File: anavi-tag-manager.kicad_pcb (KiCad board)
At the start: 2 copper layers, 74.9 x 40.6 mm, 22 parts, among them P1 CONN_01X03, U1 I2C_SENS_1, U2 I2C_SENS_1, U3 I2C_SENS_1

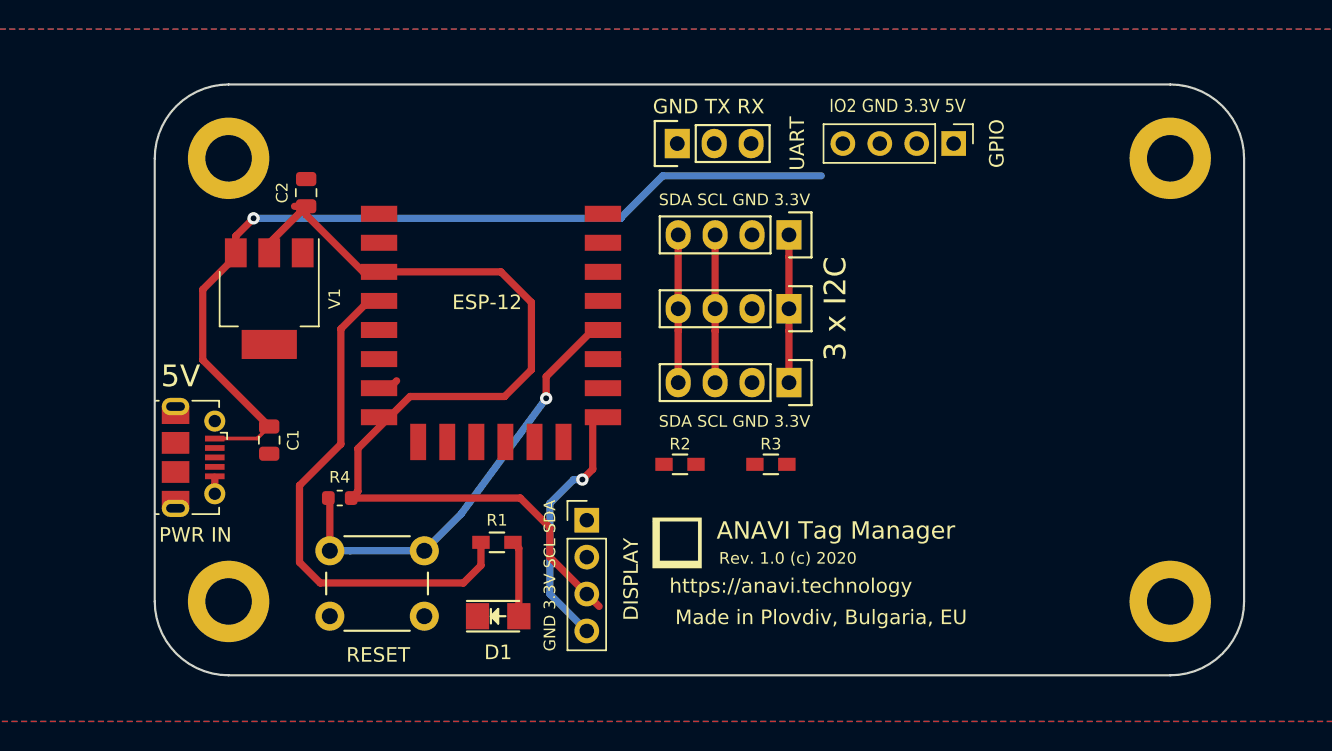
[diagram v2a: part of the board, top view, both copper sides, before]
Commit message: anavi-tag-manager.kicad_pcb: Import netlist
Signed-off-by: Leon Anavi <leon@anavi.org>
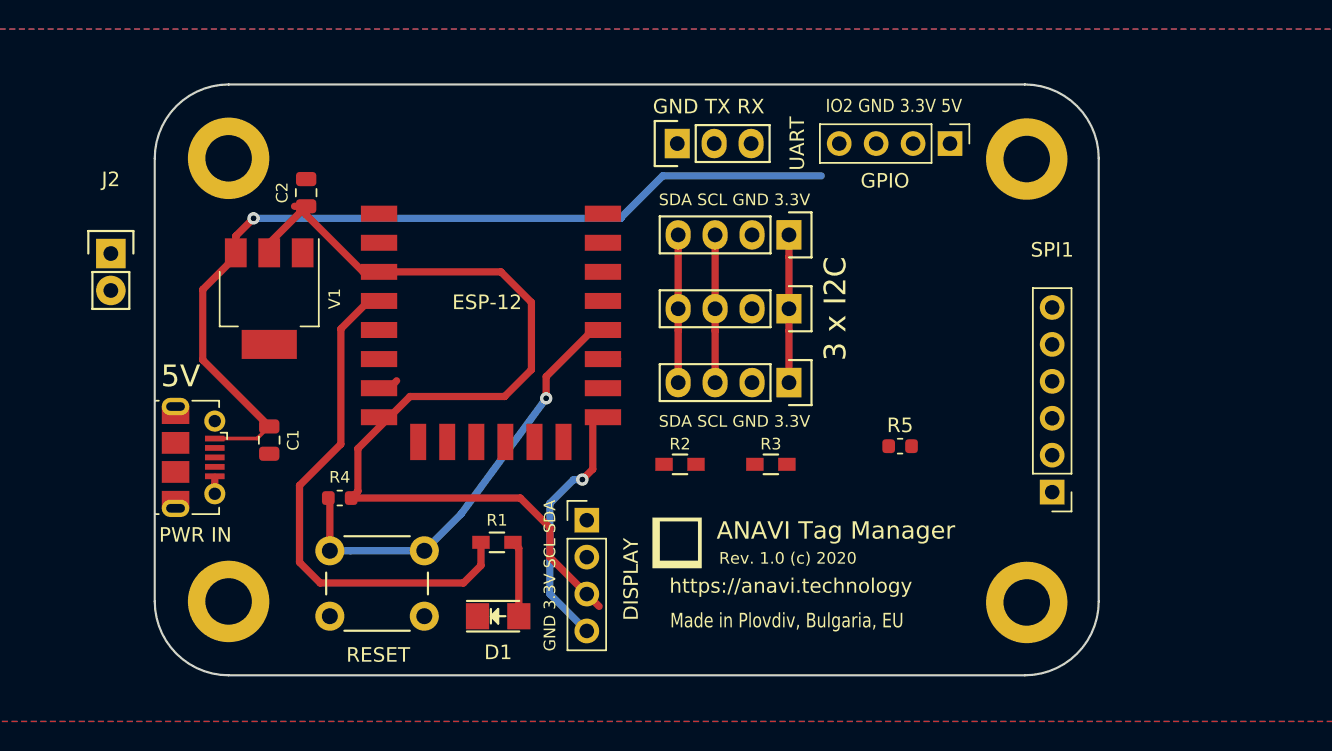
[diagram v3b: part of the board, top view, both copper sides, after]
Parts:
- removed the REF** at (134.6, 76.2)
- removed the REF** at (134.6, 106.7)
- added J2: Conn_01x02, Pin_Headers:Pin_Header_Straight_1x02, F.Cu at (61.8, 82.8)
- added R5: 4,7K, Resistor_SMD:R_0603_1608Metric, F.Cu at (116.0, 96.0)
- added REF**: MountingHole_3.2mm_M3_DIN965_Pad, Mounting_Holes:MountingHole_3.2mm_M3_DIN965_Pad, F.Cu at (124.8, 76.2)
- added REF**: MountingHole_3.2mm_M3_DIN965_Pad, Mounting_Holes:MountingHole_3.2mm_M3_DIN965_Pad, F.Cu at (124.8, 106.8)
- added SPI1: Conn_01x06, Connector_PinHeader_2.54mm:PinHeader_1x06_P2.54mm_Vertical, F.Cu at (126.5, 99.2)
- moved GPIO 0.25 mm to (119.5, 75.2)
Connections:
- ESP-12 pad 1: Net-(ESP-12-Pad1) -> (no net)
- ESP-12 pad 10: GND -> Net-(ESP-12-Pad10)
- ESP-12 pad 17: Net-(ESP-12-Pad17) -> (no net)
- ESP-12 pad 18: Net-(ESP-12-Pad18) -> (no net)
- ESP-12 pad 19: Net-(ESP-12-Pad19) -> (no net)
- ESP-12 pad 2: Net-(ESP-12-Pad2) -> (no net)
- ESP-12 pad 20: Net-(ESP-12-Pad20) -> (no net)
- ESP-12 pad 21: Net-(ESP-12-Pad21) -> (no net)
- ESP-12 pad 22: Net-(ESP-12-Pad22) -> (no net)
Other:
- board size 74.9 x 40.6 mm -> 64.9 x 40.6 mm

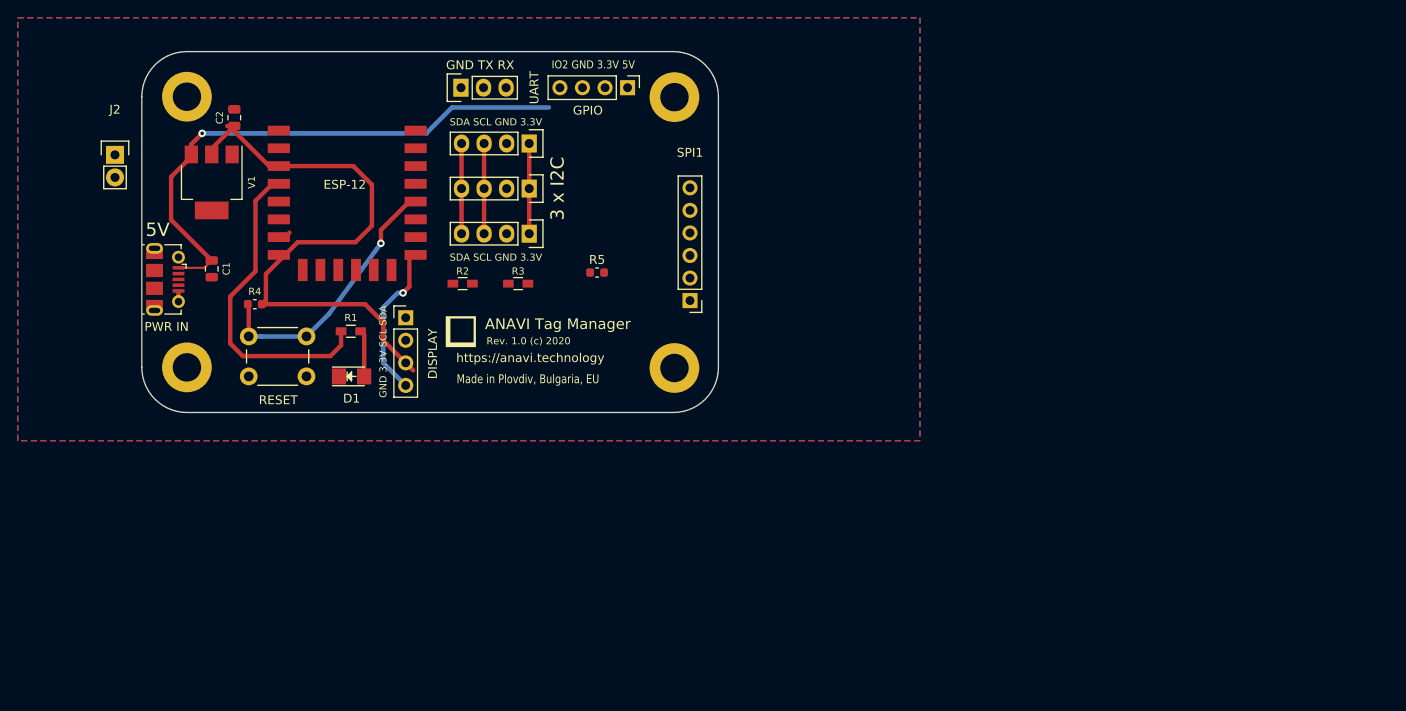
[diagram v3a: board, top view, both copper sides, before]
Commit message: anavi-tag-manager.kicad_pcb: PCB routing
Apart from the routing, also change the position of GND on the
GPIO header (with IO2). The new order makes connecting servo
motors easier because the yellow wire should go to IO2, red wire
to 5V and black wire to GND.

Signed-off-by: Leon Anavi <leon@anavi.org>
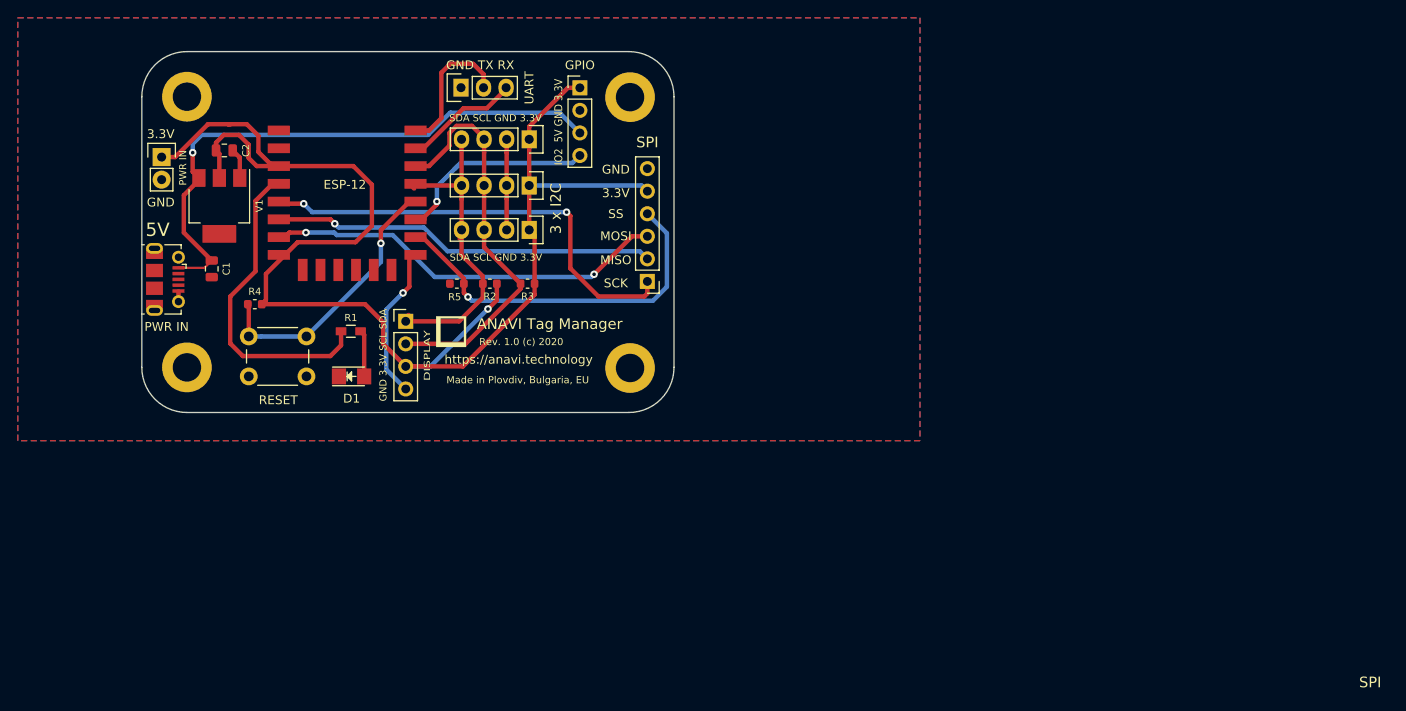
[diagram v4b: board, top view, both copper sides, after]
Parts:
- removed SPI1: Conn_01x06, Connector_PinHeader_2.54mm:PinHeader_1x06_P2.54mm_Vertical
- added ?: , , F.Cu at (121.8, 81.0)
- added SPI: Conn_01x06, Connector_PinHeader_2.54mm:PinHeader_1x06_P2.54mm_Vertical, F.Cu at (121.7, 97.0)
- PWR IN: renamed from J2
- R2, R3: footprint Resistors_SMD:R_0603_HandSoldering -> Resistor_SMD:R_0603_1608Metric
- moved R5 15.8 mm to (100.2, 97.2), turned to 180 degrees
- moved GPIO 5.37 mm to (114.1, 75.2), turned to 0 degrees
- moved PWR IN 5.26 mm to (67.0, 83.0)
- moved REF** 5.00 mm to (119.8, 76.2)
- moved REF** 5.00 mm to (119.8, 106.8)
- moved C2 3.85 mm to (74.1, 82.2), turned to 0 degrees
- moved R2 3.06 mm to (104.0, 97.3)
- moved V1 2.78 mm to (73.5, 88.5)
- moved G*** 1.10 mm to (99.6, 102.7)
- moved R3 1.06 mm to (108.2, 97.3)
- moved U3 0.47 mm to (108.4, 81.0)
- moved U1 0.43 mm to (108.4, 91.2)
- moved DISPLAY 0.40 mm to (94.5, 101.5)
- moved U2 0.35 mm to (108.4, 86.2)
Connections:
- GPIO pad 1: +5V -> +3V3
- GPIO pad 2: +3V3 -> GND
- GPIO pad 3: GND -> +5V
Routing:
- net +3V3: track 77.9 -> 163.2 mm, vias 0 -> 1
- net Net-(ESP-12-Pad5): track 0.00 -> 50.2 mm, vias 0 -> 2
- net Net-(ESP-12-Pad7): track 0.72 -> 45.7 mm, vias 0 -> 2
- net Net-(ESP-12-Pad10): track 0.00 -> 44.1 mm, vias 0 -> 1
- net Net-(ESP-12-Pad6): track 0.00 -> 42.6 mm, vias 0 -> 1
- net Net-(ESP-12-Pad14): track 10.5 -> 47.4 mm
- net Net-(ESP-12-Pad13): track 11.2 -> 36.4 mm
- net Net-(ESP-12-Pad11): track 3.12 -> 25.5 mm, vias 0 -> 1
- net Net-(ESP-12-Pad16): track 0.00 -> 16.5 mm
- net Net-(ESP-12-Pad15): track 0.00 -> 13.8 mm
- net GND: track 18.5 -> 31.9 mm
- net +5V: track 62.6 -> 66.0 mm
- net Net-(ESP-12-Pad12): track 29.7 -> 30.2 mm
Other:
- board size 64.9 x 40.6 mm -> 59.9 x 40.6 mm
- board text added: "3.3V"
- board text added: "GND"
- board text added: "IO2 5V GND 3.3V"
- board text added: "MISO"
- board text added: "MOSI"
- board text added: "SCK"
- board text added: "SS"
- board text removed: "IO2 GND 3.3V 5V"

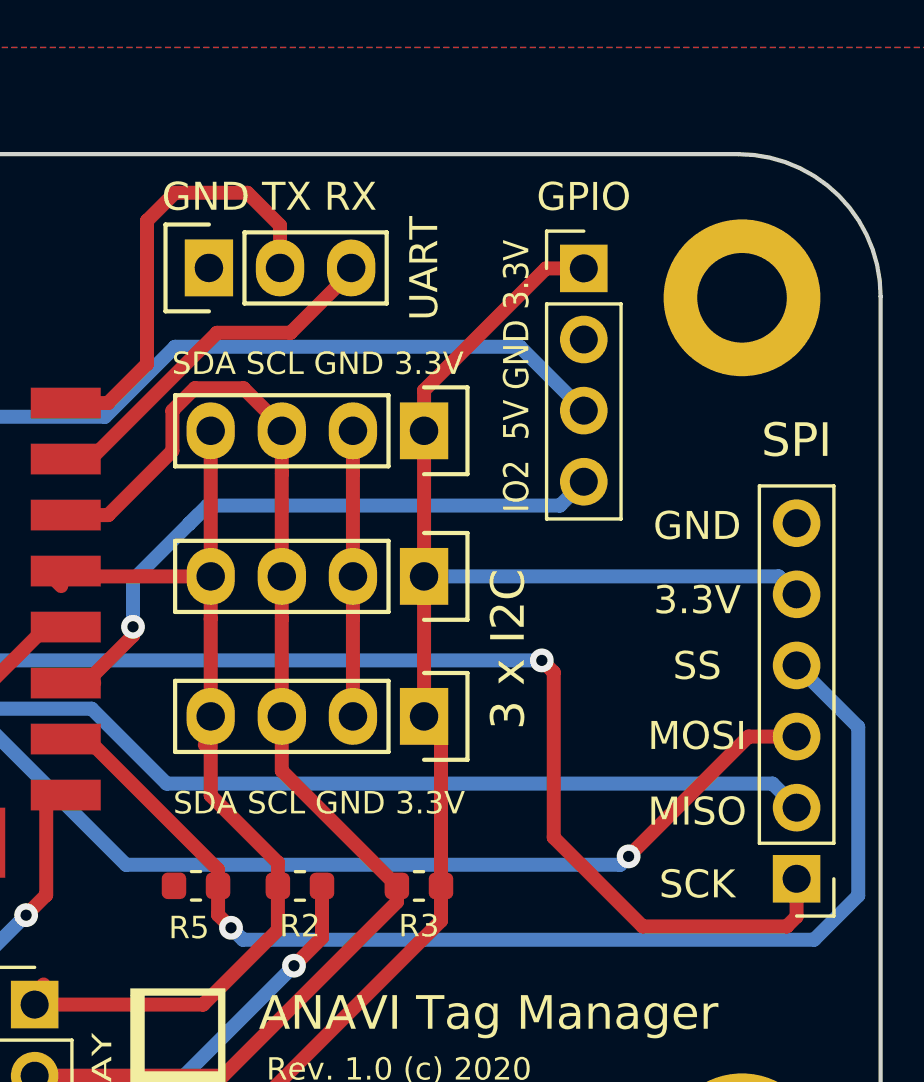
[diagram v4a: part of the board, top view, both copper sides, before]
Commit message: anavi-tag-manager.kicad_pcb: Adjust positions
Adjust positions of components.

Signed-off-by: Leon Anavi <leon@anavi.org>
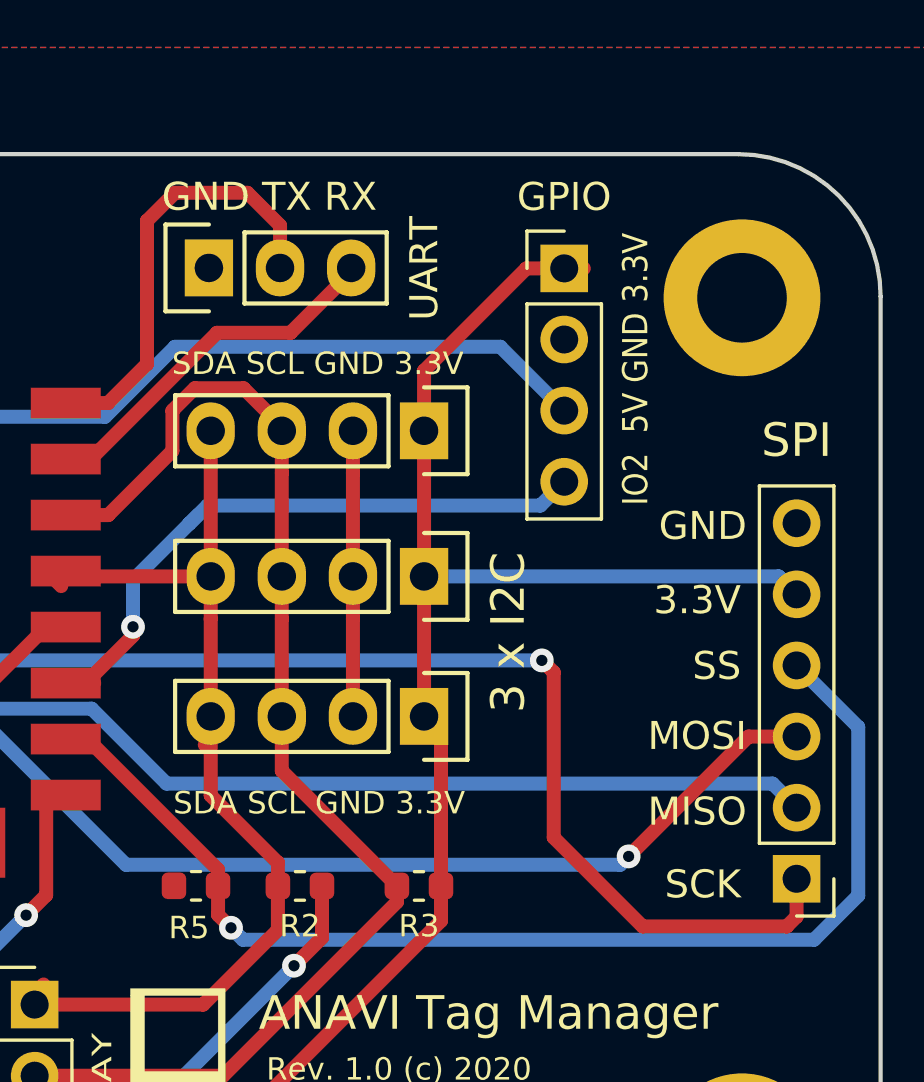
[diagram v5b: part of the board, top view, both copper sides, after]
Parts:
- moved GPIO 0.70 mm to (113.4, 75.2)
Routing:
- net Net-(ESP-12-Pad11): track 25.5 -> 24.8 mm
- net +5V: track 66.0 -> 65.3 mm
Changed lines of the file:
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@@
   )
   (module Connector_PinHeader_2.54mm:PinHeader_1x04_P2.54mm_Vertical (layer F.Cu)
-    (at 114.1 75.2)
+    (at 113.4 75.2)
     (descr "Through hole straight pin header, 1x04, 2.54mm pitch, single row")
     (tags "Through hole pin header THT 1x04 2.54mm single row")
@@
     (effects (font (size 1 1) (thickness 0.15)))
   )
-  (gr_text GND (at 118.15 84.4) (layer F.SilkS)
+  (gr_text GND (at 118.35 84.4) (layer F.SilkS)
     (effects (font (size 1 1) (thickness 0.15)))
   )
@@
     (effects (font (size 1 1) (thickness 0.15)))
   )
-  (gr_text SS (at 118.15 89.4) (layer F.SilkS)
+  (gr_text SS (at 118.85 89.4) (layer F.SilkS)
     (effects (font (size 1 1) (thickness 0.15)))
   )
@@
     (effects (font (size 1 1) (thickness 0.15)))
   )
-  (gr_text SCK (at 118.15 97.2) (layer F.SilkS)
+  (gr_text SCK (at 118.35 97.2) (layer F.SilkS)
     (effects (font (size 1 1) (thickness 0.15)))
   )
@@
     (effects (font (size 0.8 0.8) (thickness 0.15)))
   )
-  (gr_text "IO2  5V GND 3.3V" (at 111.7 79.05 90) (layer F.SilkS)
+  (gr_text "IO2  5V GND 3.3V" (at 115.95 78.8 90) (layer F.SilkS)
     (effects (font (size 0.9 0.8) (thickness 0.15)))
   )
@@
     (effects (font (size 1 1) (thickness 0.2)))
   )
-  (gr_text "3 x I2C" (at 111.4 88.8 90) (layer F.SilkS)
+  (gr_text "3 x I2C" (at 111.4 88.2 90) (layer F.SilkS)
     (effects (font (size 1.2 1.2) (thickness 0.25)))
   )
@@
   (segment (start 114.0421 75.2) (end 114.1 75.2) (width 0.5) (layer F.Cu) (net 3))
   (segment (start 108.3945 81) (end 108.3945 80.8476) (width 0.5) (layer F.Cu) (net 3))
-  (segment (start 112.75 75.2) (end 114.1 75.2) (width 0.5) (layer F.Cu) (net 3))
-  (segment (start 108.3945 79.5555) (end 112.75 75.2) (width 0.5) (layer F.Cu) (net 3))
-  (segment (start 108.3945 81) (end 108.3945 79.5555) (width 0.5) (layer F.Cu) (net 3))
+  (segment (start 112.05 75.2) (end 113.4 75.2) (width 0.5) (layer F.Cu) (net 3))
+  (segment (start 108.3945 78.8555) (end 112.05 75.2) (width 0.5) (layer F.Cu) (net 3))
+  (segment (start 108.3945 81) (end 108.3945 78.8555) (width 0.5) (layer F.Cu) (net 3))
   (segment (start 100.5635 92.219) (end 100.7745 92.008) (width 0.5) (layer F.Cu) (net 4))
   (segment (start 100.754 81.4465) (end 100.7745 81.467) (width 0.5) (layer F.Cu) (net 4))
@@
   (segment (start 71.2 85.35) (end 70.5 84.65) (width 0.5) (layer F.Cu) (net 11))
   (segment (start 70.5 84.65) (end 70.5 82.5) (width 0.5) (layer F.Cu) (net 11))
-  (segment (start 111.82 78) (end 114.1 80.28) (width 0.5) (layer B.Cu) (net 11))
   (segment (start 70.5 82.5) (end 70.5 81.5) (width 0.5) (layer B.Cu) (net 11))
-  (segment (start 99.5 78) (end 111.82 78) (width 0.5) (layer B.Cu) (net 11))
   (segment (start 97 80.5) (end 99.5 78) (width 0.5) (layer B.Cu) (net 11))
   (segment (start 71.5 80.5) (end 97 80.5) (width 0.5) (layer B.Cu) (net 11))
   (segment (start 70.5 81.5) (end 71.5 80.5) (width 0.5) (layer B.Cu) (net 11))
+  (segment (start 111.12 78) (end 113.4 80.28) (width 0.5) (layer B.Cu) (net 11))
+  (segment (start 99.5 78) (end 111.12 78) (width 0.5) (layer B.Cu) (net 11))
   (segment (start 96.306202 90.01) (end 94.899 90.01) (width 0.5) (layer F.Cu) (net 12))
   (segment (start 94.899 90.01) (end 96.614 90.01) (width 0.5) (layer F.Cu) (net 12))
@@
   (segment (start 100 84.327992) (end 100.327992 84) (width 0.5) (layer B.Cu) (net 12))
   (segment (start 98 86.327992) (end 100 84.327992) (width 0.5) (layer B.Cu) (net 12))
-  (segment (start 113.250001 83.669999) (end 114.1 82.82) (width 0.5) (layer B.Cu) (net 12))
-  (segment (start 100.657993 83.669999) (end 113.250001 83.669999) (width 0.5) (layer B.Cu) (net 12))
+  (segment (start 112.550001 83.669999) (end 113.4 82.82) (width 0.5) (layer B.Cu) (net 12))
+  (segment (start 100.657993 83.669999) (end 112.550001 83.669999) (width 0.5) (layer B.Cu) (net 12))
   (via (at 83 88.25) (size 0.85) (drill 0.4) (layers F.Cu B.Cu) (net 13))
   (segment (start 81.139 88.25) (end 80.899 88.01) (width 0.5) (layer F.Cu) (net 13))

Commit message: anavi-tag-manager.kicad_pcb: Set R5 to 2K
Change R5 value from 4.7K to 2K to ensure that the PN532 NFC
module will not affect the initial state of GPIO15 on booting.

Signed-off-by: Leon Anavi <leon@anavi.org>
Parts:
- added ?: , , F.Cu at (106.9, 95.7)
- R5: value 4,7K -> 2K
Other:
- board text added: "ESP-12E"
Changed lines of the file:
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@@
   (general
     (thickness 1.6)
-    (drawings 29)
+    (drawings 30)
     (tracks 212)
     (zones 0)
-    (modules 26)
+    (modules 27)
     (nets 16)
   )
@@
   )
   (module "" (layer F.Cu)
+    (at 106.9 95.7)
+    (fp_text reference "" (at 121.8 81) (layer F.SilkS)
+      (effects (font (size 1.27 1.27) (thickness 0.15)))
+    )
+    (fp_text value "" (at 121.8 81) (layer F.SilkS)
+      (effects (font (size 1.27 1.27) (thickness 0.15)))
+    )
+    (fp_text user 4,7K (at 137.0125 92.325001) (layer F.Fab)
+      (effects (font (size 1 1) (thickness 0.15)))
+    )
+  )
+  (module "" (layer F.Cu)
     (at 121.8 81)
     (fp_text reference "" (at 80.899 80.01) (layer F.SilkS)
@@
       (effects (font (size 0.8 0.8) (thickness 0.15)))
     )
-    (fp_text value 4,7K (at 0 1.5 180) (layer F.Fab)
+    (fp_text value 2K (at 0 1.5 180) (layer F.Fab)
       (effects (font (size 1 1) (thickness 0.15)))
     )
@@
     )
   )
+  (gr_text ESP-12E (at 87.7 82.4) (layer F.Fab)
+    (effects (font (size 1.5 1.5) (thickness 0.3)))
+  )
   (gr_text GND (at 66.9 88.1) (layer F.SilkS)
